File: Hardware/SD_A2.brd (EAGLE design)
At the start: 100 x 80 mm, 24 parts, among them IC1 74HCT245N, IC2 LM317, IC3 2716

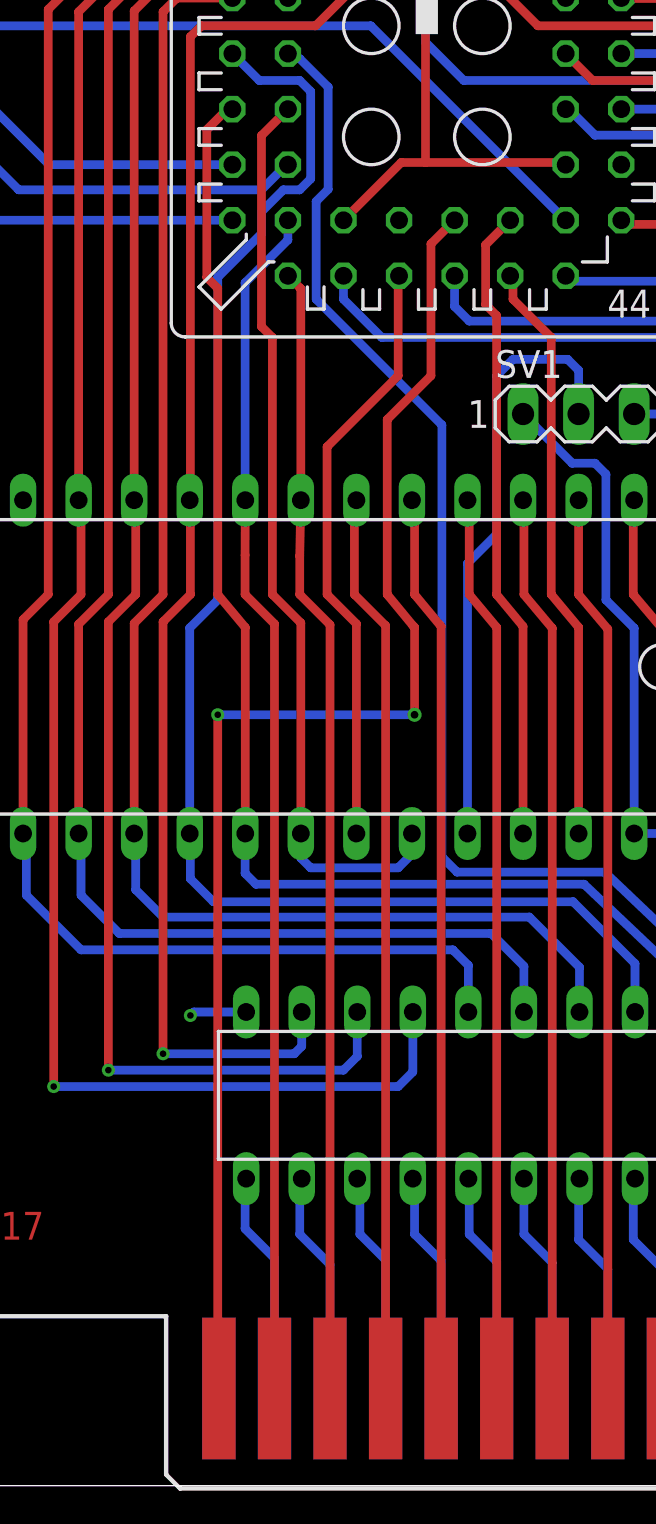
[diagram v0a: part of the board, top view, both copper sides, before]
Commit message: Pinning changed
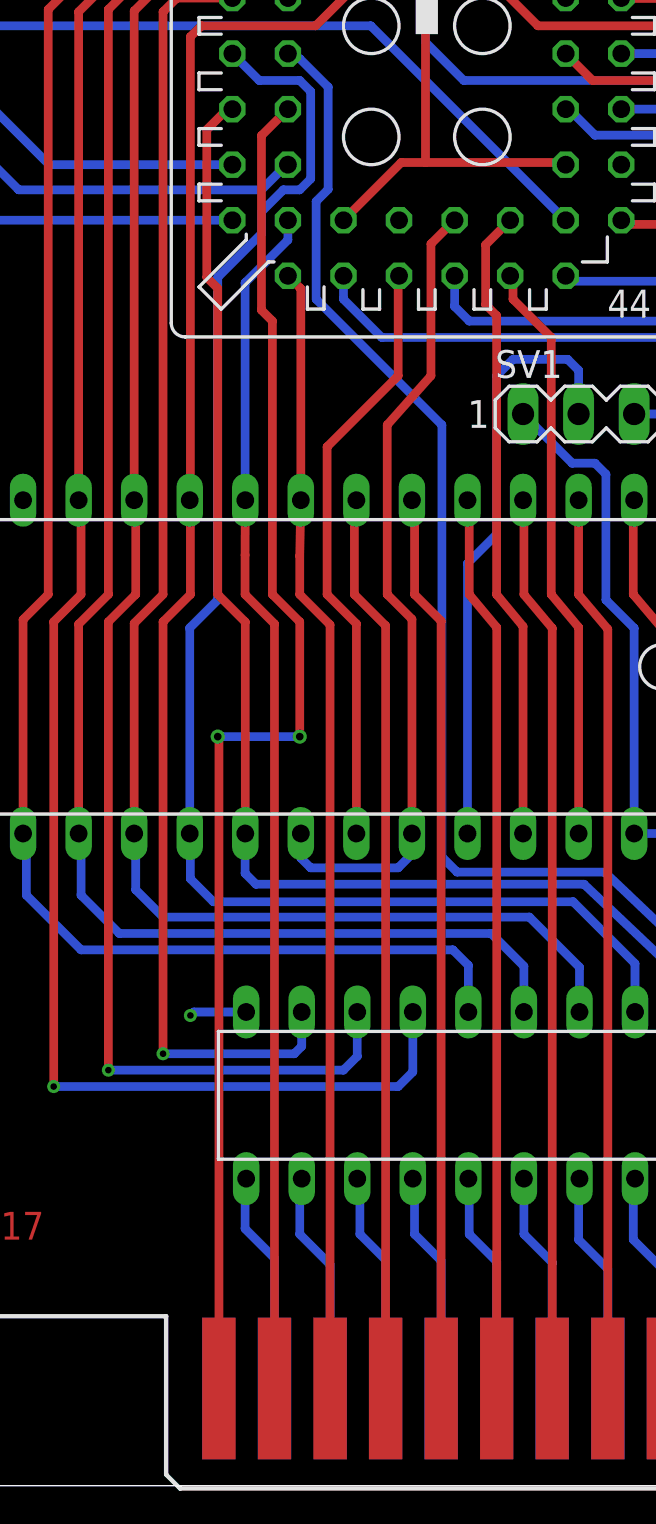
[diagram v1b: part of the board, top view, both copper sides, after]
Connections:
- net A10_B renamed B10
- net A8_B renamed B8
- net A9_B renamed B9
- net !IO_SEL: now also U$1.14; no longer U$1.25
- net !OE: now also U$1.25; no longer U$1.14
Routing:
- net !OE: track 42.0 -> 37.3 mm
- net !IO_SEL: track 64.2 -> 63.5 mm
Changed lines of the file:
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@@
 <wire x1="44.9441875" y1="28.0558125" x2="45" y2="28" width="0.4" layer="16"/>
 </signal>
-<signal name="A10_B">
+<signal name="B10">
 <contactref element="IC3" pad="19"/>
 <wire x1="33.59" y1="29.82" x2="33.59" y2="39.41" width="0.4" layer="1"/>
@@
 <wire x1="32.25" y1="40.75" x2="32.25" y2="47.5" width="0.4" layer="1"/>
 </signal>
-<signal name="A9_B">
+<signal name="B9">
 <contactref element="IC3" pad="22"/>
 <wire x1="41.21" y1="29.82" x2="41.21" y2="39.29" width="0.4" layer="1"/>
@@
 <wire x1="39.5" y1="56.74" x2="40.62" y2="57.86" width="0.4" layer="1"/>
 </signal>
-<signal name="A8_B">
+<signal name="B8">
 <contactref element="IC3" pad="23"/>
 <wire x1="43.75" y1="29.82" x2="43.75" y2="39.25" width="0.4" layer="1"/>
@@
 <wire x1="40.75" y1="55.19" x2="40.62" y2="55.32" width="0.4" layer="1"/>
 <wire x1="42.5" y1="52.5" x2="40.75" y2="54.25" width="0.4" layer="1"/>
-</signal>
-<signal name="!OE">
-<contactref element="U$1" pad="14"/>
-<contactref element="IC3" pad="20"/>
-<wire x1="31.05" y1="39.45" x2="29.75" y2="40.75" width="0.4" layer="1"/>
-<wire x1="35.5" y1="28.25" x2="31.5" y2="28.25" width="0.4" layer="16"/>
-<wire x1="31.05" y1="28.7" x2="31.5" y2="28.25" width="0.4" layer="16"/>
-<wire x1="29.75" y1="52.5" x2="29.25" y2="53" width="0.4" layer="1"/>
-<wire x1="29.25" y1="53" x2="29.25" y2="61.73" width="0.4" layer="1"/>
-<wire x1="29.25" y1="61.73" x2="30.46" y2="62.94" width="0.4" layer="1"/>
-<wire x1="29.75" y1="40.75" x2="29.75" y2="52.5" width="0.4" layer="1"/>
-<contactref element="IC3" pad="18"/>
-<wire x1="31.05" y1="29.82" x2="31.05" y2="28.7" width="0.4" layer="16"/>
-<wire x1="31.05" y1="29.82" x2="31.05" y2="39.45" width="0.4" layer="1"/>
-<wire x1="36.13" y1="29.82" x2="36.13" y2="28.88" width="0.4" layer="16"/>
-<wire x1="36.13" y1="28.88" x2="35.5" y2="28.25" width="0.4" layer="16"/>
 </signal>
 <signal name="N$5">
@@
 <contactref element="ST1" pad="05"/>
 <contactref element="IC3" pad="5"/>
-<wire x1="37.465" y1="39.285" x2="36.25" y2="40.75" width="0.4" layer="1"/>
+<wire x1="37.465" y1="39.535" x2="36.25" y2="40.75" width="0.4" layer="1"/>
 <wire x1="36.25" y1="40.75" x2="36.25" y2="44.94" width="0.4" layer="1"/>
 <wire x1="36.25" y1="44.94" x2="36.13" y2="45.06" width="0.4" layer="1"/>
-<wire x1="37.465" y1="4.445" x2="37.465" y2="39.285" width="0.4" layer="1"/>
+<wire x1="37.465" y1="4.445" x2="37.465" y2="39.535" width="0.4" layer="1"/>
 </signal>
 <signal name="ADD4">
@@
 <wire x1="28.5" y1="28" x2="28.5" y2="29.81" width="0.4" layer="16"/>
 <wire x1="28.5" y1="29.81" x2="28.51" y2="29.82" width="0.4" layer="16"/>
-<wire x1="28.51" y1="29.82" x2="28.51" y2="39.24" width="0.4" layer="1"/>
+<wire x1="28.51" y1="29.82" x2="28.51" y2="39.49" width="0.4" layer="1"/>
 <wire x1="48.87" y1="22.88" x2="48.87" y2="21.66" width="0.4" layer="16"/>
-<wire x1="28.51" y1="39.24" x2="27.25" y2="40.75" width="0.4" layer="1"/>
+<wire x1="28.51" y1="39.49" x2="27.25" y2="40.75" width="0.4" layer="1"/>
 <wire x1="27.25" y1="40.75" x2="27.25" y2="54.75" width="0.4" layer="1"/>
 <wire x1="27.25" y1="54.75" x2="26.75" y2="55.25" width="0.4" layer="1"/>
@@
 <wire x1="45.75" y1="73" x2="43.26" y2="73" width="0.4" layer="1"/>
 <wire x1="43.26" y1="73" x2="43.16" y2="73.1" width="0.4" layer="1"/>
-</signal>
-<signal name="!IO_SEL">
-<wire x1="36.17" y1="39.33" x2="35" y2="40.75" width="0.4" layer="1"/>
-<contactref element="ST1" pad="01"/>
-<via x="27.25" y="35.25" extent="1-16" drill="0.3" diameter="0.6"/>
-<wire x1="27.25" y1="35.25" x2="27.25" y2="4.5" width="0.4" layer="1"/>
-<wire x1="27.25" y1="4.5" x2="27.305" y2="4.445" width="0.4" layer="1"/>
-<contactref element="U$1" pad="25"/>
-<wire x1="37" y1="56.78" x2="38.08" y2="57.86" width="0.4" layer="1"/>
-<wire x1="27.25" y1="35.25" x2="36.25" y2="35.25" width="0.4" layer="16"/>
-<via x="36.25" y="35.25" extent="1-16" drill="0.35"/>
-<wire x1="36.25" y1="35.25" x2="36.25" y2="39.25" width="0.4" layer="1"/>
-<wire x1="36.25" y1="39.25" x2="36.17" y2="39.33" width="0.4" layer="1"/>
-<wire x1="35" y1="40.75" x2="35" y2="48.75" width="0.4" layer="1"/>
-<wire x1="35" y1="48.75" x2="37" y2="50.75" width="0.4" layer="1"/>
-<wire x1="37" y1="50.75" x2="37" y2="56.78" width="0.4" layer="1"/>
 </signal>
 <signal name="!DEV_SEL">
@@
 <wire x1="57.85" y1="61.1" x2="57.85" y2="58.98075625" width="0.4" layer="1"/>
 </signal>
+<signal name="!OE">
+<contactref element="U$1" pad="25"/>
+<contactref element="IC3" pad="20"/>
+<contactref element="IC3" pad="18"/>
+<wire x1="37" y1="56.78" x2="38.08" y2="57.86" width="0.4" layer="1"/>
+<wire x1="37" y1="50.75" x2="35" y2="48.5" width="0.4" layer="1"/>
+<wire x1="37" y1="50.75" x2="37" y2="56.78" width="0.4" layer="1"/>
+<wire x1="35.5" y1="28.25" x2="31.5" y2="28.25" width="0.4" layer="16"/>
+<wire x1="31.05" y1="28.7" x2="31.5" y2="28.25" width="0.4" layer="16"/>
+<wire x1="31.05" y1="29.82" x2="31.05" y2="28.7" width="0.4" layer="16"/>
+<wire x1="36.13" y1="29.82" x2="36.13" y2="28.88" width="0.4" layer="16"/>
+<wire x1="36.13" y1="28.88" x2="35.5" y2="28.25" width="0.4" layer="16"/>
+<wire x1="35" y1="40.75" x2="35" y2="48.5" width="0.4" layer="1"/>
+<wire x1="36.13" y1="29.82" x2="36.13" y2="39.62" width="0.4" layer="1"/>
+<wire x1="36.13" y1="39.62" x2="35" y2="40.75" width="0.4" layer="1"/>
+</signal>
+<signal name="!IO_SEL">
+<contactref element="U$1" pad="14"/>
+<contactref element="ST1" pad="01"/>
+<wire x1="27.305" y1="4.445" x2="27.305" y2="34.195" width="0.4" layer="1"/>
+<wire x1="27.305" y1="34.195" x2="27.25" y2="34.25" width="0.4" layer="1"/>
+<via x="27.25" y="34.25" extent="1-16" drill="0.35"/>
+<wire x1="27.25" y1="34.25" x2="31" y2="34.25" width="0.4" layer="16"/>
+<via x="31" y="34.25" extent="1-16" drill="0.35"/>
+<wire x1="31" y1="34.25" x2="31" y2="39.5" width="0.4" layer="1"/>
+<wire x1="31" y1="39.5" x2="29.75" y2="40.75" width="0.4" layer="1"/>
+<wire x1="29.75" y1="40.75" x2="29.75" y2="53.25" width="0.4" layer="1"/>
+<wire x1="29.75" y1="53.25" x2="29.25" y2="53.75" width="0.4" layer="1"/>
+<wire x1="29.25" y1="53.75" x2="29.25" y2="61.73" width="0.4" layer="1"/>
+<wire x1="29.25" y1="61.73" x2="30.46" y2="62.94" width="0.4" layer="1"/>
+</signal>
 </signals>

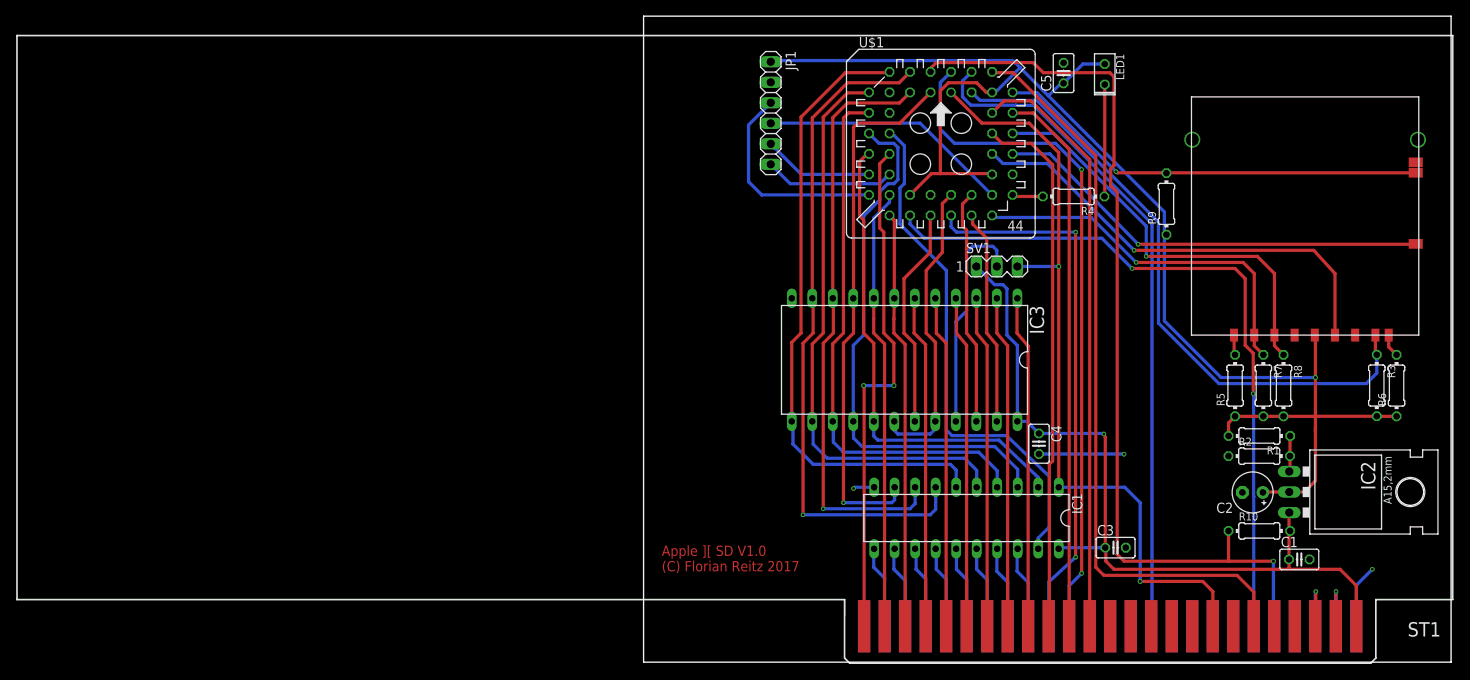
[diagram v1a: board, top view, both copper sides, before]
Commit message: !CE on GND
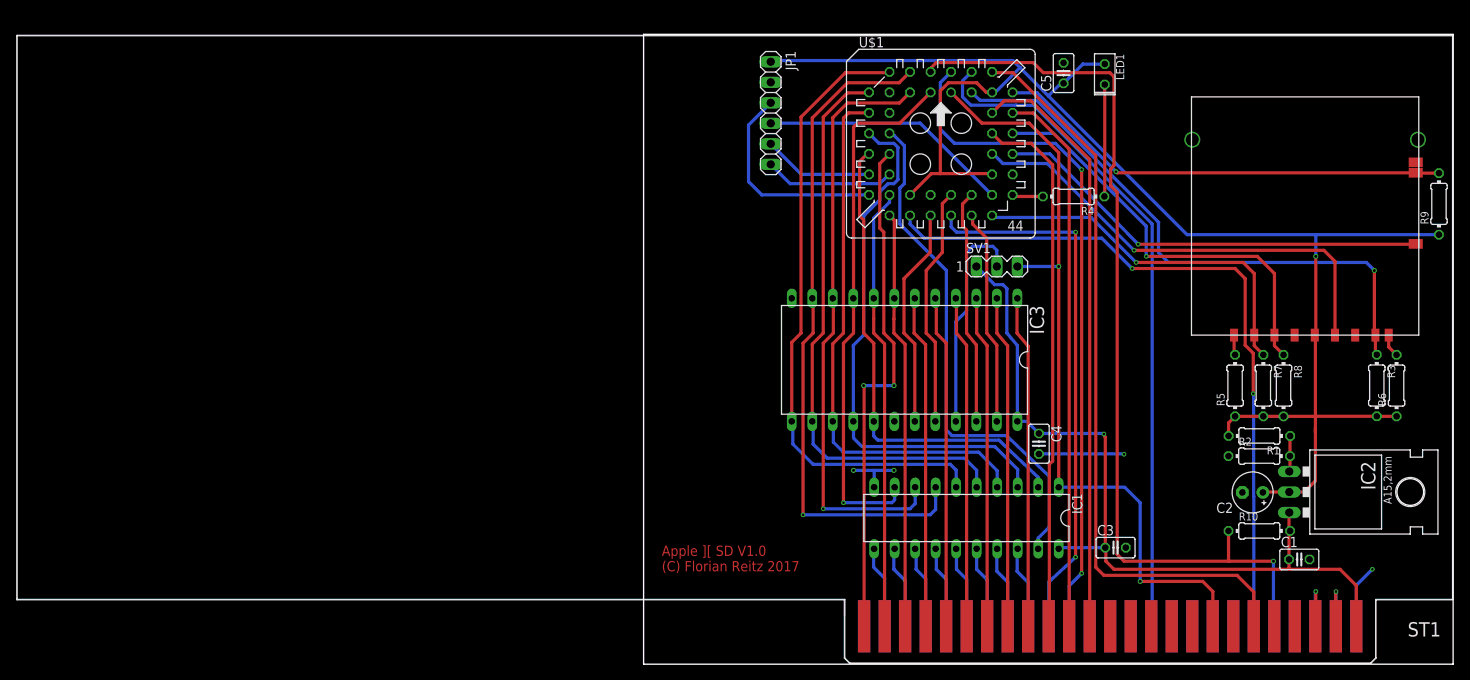
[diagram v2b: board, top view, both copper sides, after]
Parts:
- moved R9 33.8 mm to (98.5, 56.8)
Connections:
- net !OE: no longer IC3.18
- net GND: now also IC3.18
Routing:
- net +3V3: track 182.7 -> 195.0 mm
- net !OE: track 37.3 -> 29.7 mm
- net MISO: track 77.7 -> 71.8 mm, vias 0 -> 1
- net GND: track 21.0 -> 25.5 mm, vias 3 -> 4
- net WP: track 54.1 -> 56.9 mm
- net CLK: track 56.3 -> 57.1 mm
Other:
- board size 100 x 80 mm -> 100.2 x 78 mm

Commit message: Pin changes, libraries added
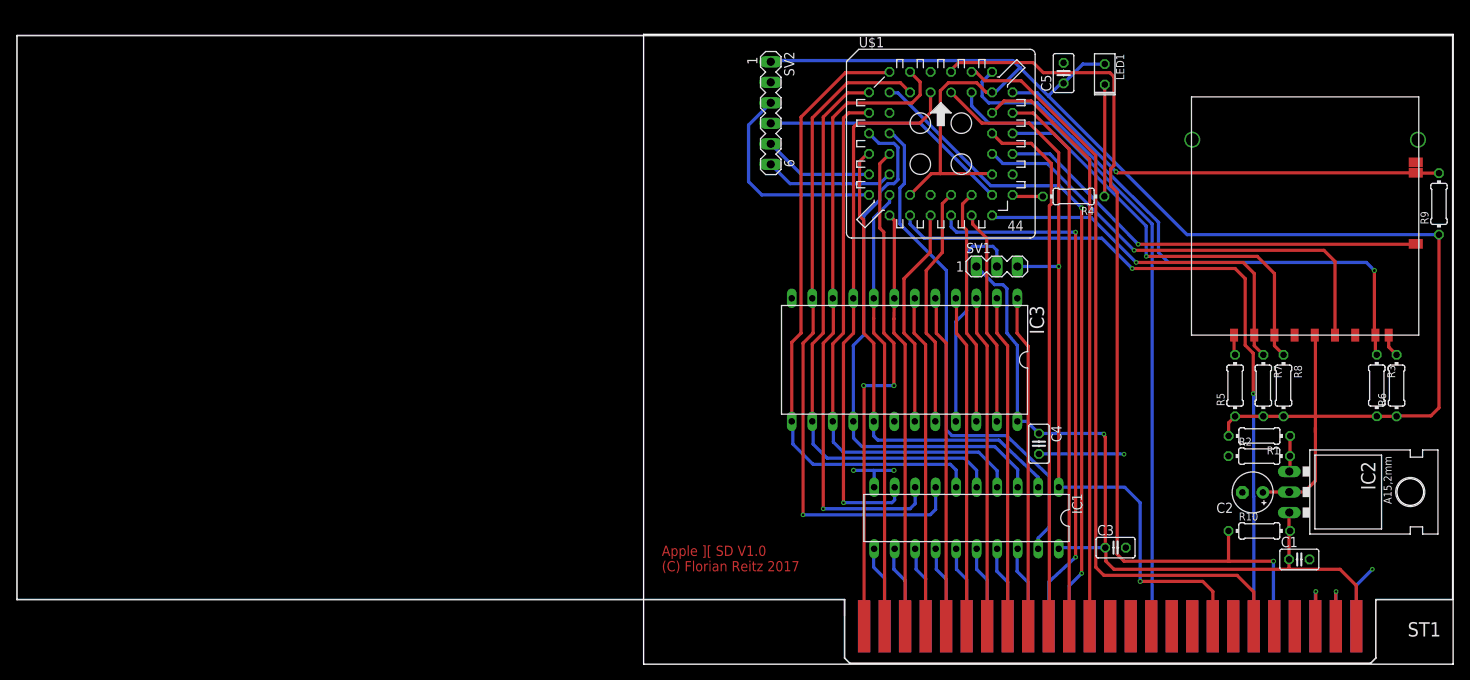
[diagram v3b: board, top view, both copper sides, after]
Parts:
- removed JP1: (no value), pinhead:1X06
- added SV2: (no value), con-lstb:MA06-1
- IC3: value 2716 -> 2716 / 2732
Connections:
- net !IO_STR: now also U$1.42; no longer U$1.40
- net !IRQ: now also U$1.44; no longer U$1.2
- net +3V3: now also SV2.1; no longer JP1.1
- net 7M: now also U$1.43; no longer U$1.42
- net DATA1: now also U$1.4; no longer U$1.5
- net DATA2: now also U$1.5; no longer U$1.4
- net GND: now also SV2.2; no longer JP1.2
- net MISO: now also U$1.40; no longer U$1.43
- net PHI_0: now also U$1.8; no longer U$1.44
- net TCK: now also SV2.3; no longer JP1.3
- net TDI: now also SV2.5; no longer JP1.5
- net TDO: now also SV2.4; no longer JP1.4
- net TMS: now also SV2.6; no longer JP1.6
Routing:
- net +3V3: track 195.0 -> 209.8 mm, vias 1 -> 0
- net DATA1: track 73.5 -> 78.0 mm
- net 7M: track 83.4 -> 80.0 mm
- net !IRQ: track 115.4 -> 112.7 mm
- net !IO_STR: track 93.2 -> 95.7 mm
- net PHI_0: track 84.4 -> 82.2 mm
- net MISO: track 71.8 -> 73.8 mm
- net DATA0: track 66.4 -> 67.9 mm

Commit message: R and C changed to SMD
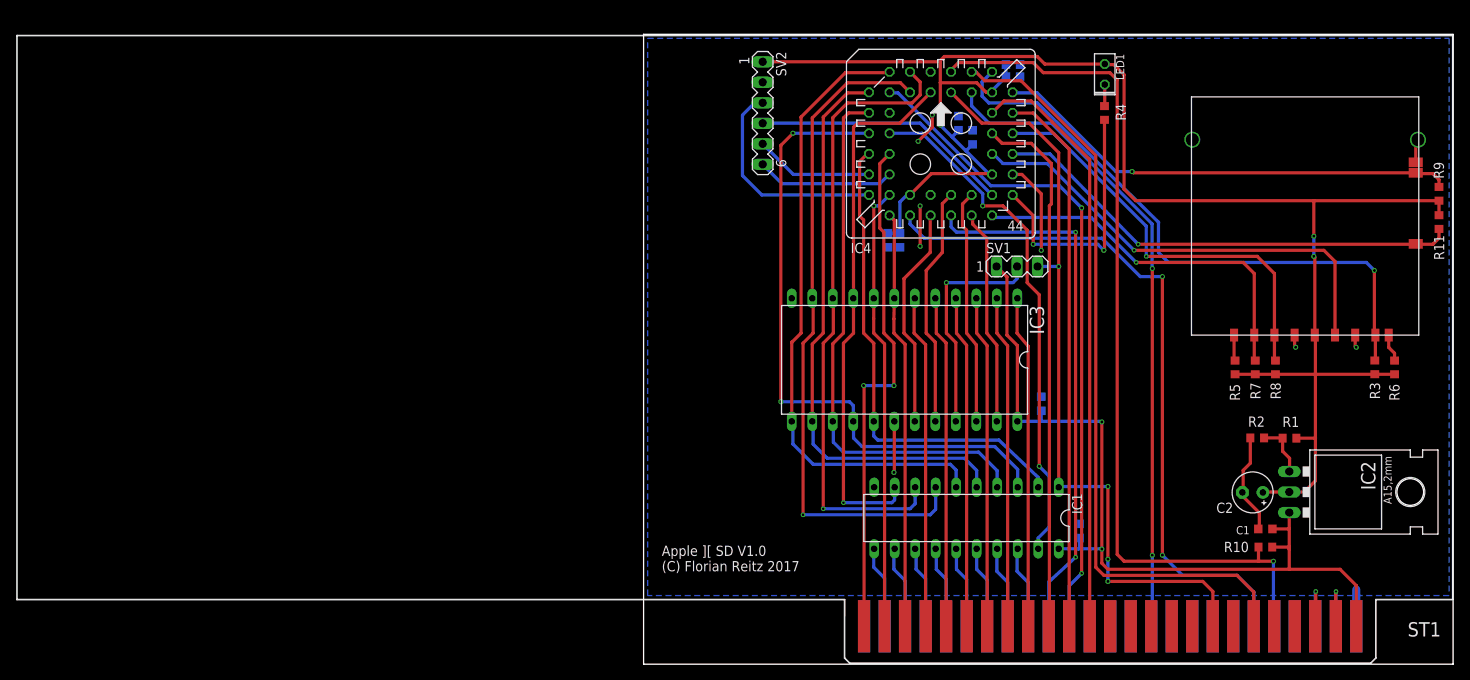
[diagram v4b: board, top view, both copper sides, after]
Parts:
- added C10, C8, C9: 10n, rcl:C0603K
- added C6, C7: 100n, rcl:C0603K
- added R11: 100k, rcl:R0603
- C1, C3, C4, C5: device rcl:C025-025X050 -> rcl:C0603K
- R1, R10, R2, R4: device rcl:0204/7 -> rcl:R0603
- R3, R5, R6, R7, R9: value 22k -> 100k; device rcl:0204/7 -> rcl:R0603
- R8: value 22k -> 68k; device rcl:0204/7 -> rcl:R0603
- moved C3 20.1 mm to (49.2, 32.0), flipped to the bottom, turned to 90 degrees
- moved C4 11.9 mm to (54.0, 16.2), flipped to the bottom, turned to 90 degrees
- moved R4 11.0 mm to (57.1, 68.0), turned to 270 degrees
- moved C5 6.35 mm to (45.8, 74.0), flipped to the bottom, turned to 180 degrees
- moved C1 5.65 mm to (77.0, 16.5), turned to 180 degrees
- moved R1 3.74 mm to (80.0, 27.7), turned to 0 degrees
- moved SV1 2.50 mm to (46.2, 49.0)
- moved R7 2.46 mm to (75.8, 36.5)
- moved R8 2.46 mm to (78.2, 36.5)
- moved R2 2.26 mm to (76.0, 27.8)
- moved R3 2.26 mm to (90.5, 36.5)
- moved R6 2.26 mm to (93.0, 36.5)
- moved R5 2.25 mm to (73.2, 36.5)
- moved R10 2.14 mm to (77.0, 14.2)
- moved R9 1.25 mm to (98.5, 58.0)
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- renumbered U$1 to IC4
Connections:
- net +3V3: now also C10.1, C6.1, C7.1, C8.1, C9.1, R11.1
- net CARD: now also R11.2
- net GND: now also C10.2, C6.2, C7.2, C8.2, C9.2, U$2.SC
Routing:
- net !LED: track 3.83 -> 32.4 mm, vias 0 -> 2
- net GND: track 25.5 -> 50.0 mm, vias 4 -> 8
- net DATA6: track 67.2 -> 80.7 mm, vias 0 -> 2
- net N$29: track 13.9 -> 2.68 mm
- net +5V: track 99.3 -> 105.4 mm, vias 1 -> 2
- net +3V3: track 209.8 -> 214.3 mm, vias 0 -> 3
- net CARD: track 54.7 -> 59.0 mm
- net N$1: track 4.45 -> 6.82 mm
- net !IRQ: track 112.7 -> 110.4 mm
- net !RESET: track 88.9 -> 87.0 mm
- net DATA0: track 67.9 -> 66.4 mm
- net WP: track 56.9 -> 58.2 mm
- net R/!W: track 97.4 -> 96.2 mm, vias 2 -> 4
- net TMS: track 16.2 -> 17.2 mm
- net TDI: track 13.7 -> 14.7 mm
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- added copper zone on layer 16, net GND

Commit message: - Gerber files
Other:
- board size 100.2 x 78 mm -> 100.2 x 77.7 mm
